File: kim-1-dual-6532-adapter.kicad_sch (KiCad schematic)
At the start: 13 parts, among them J2_1 6530_002_L, J2_2 6530_002_R, J3_1 6530_003_L, J3_2 6530_003_R, U1 27C64, U2 6532, U3 6532, U4 74LS138, U5 74LS00, U6 74LS04

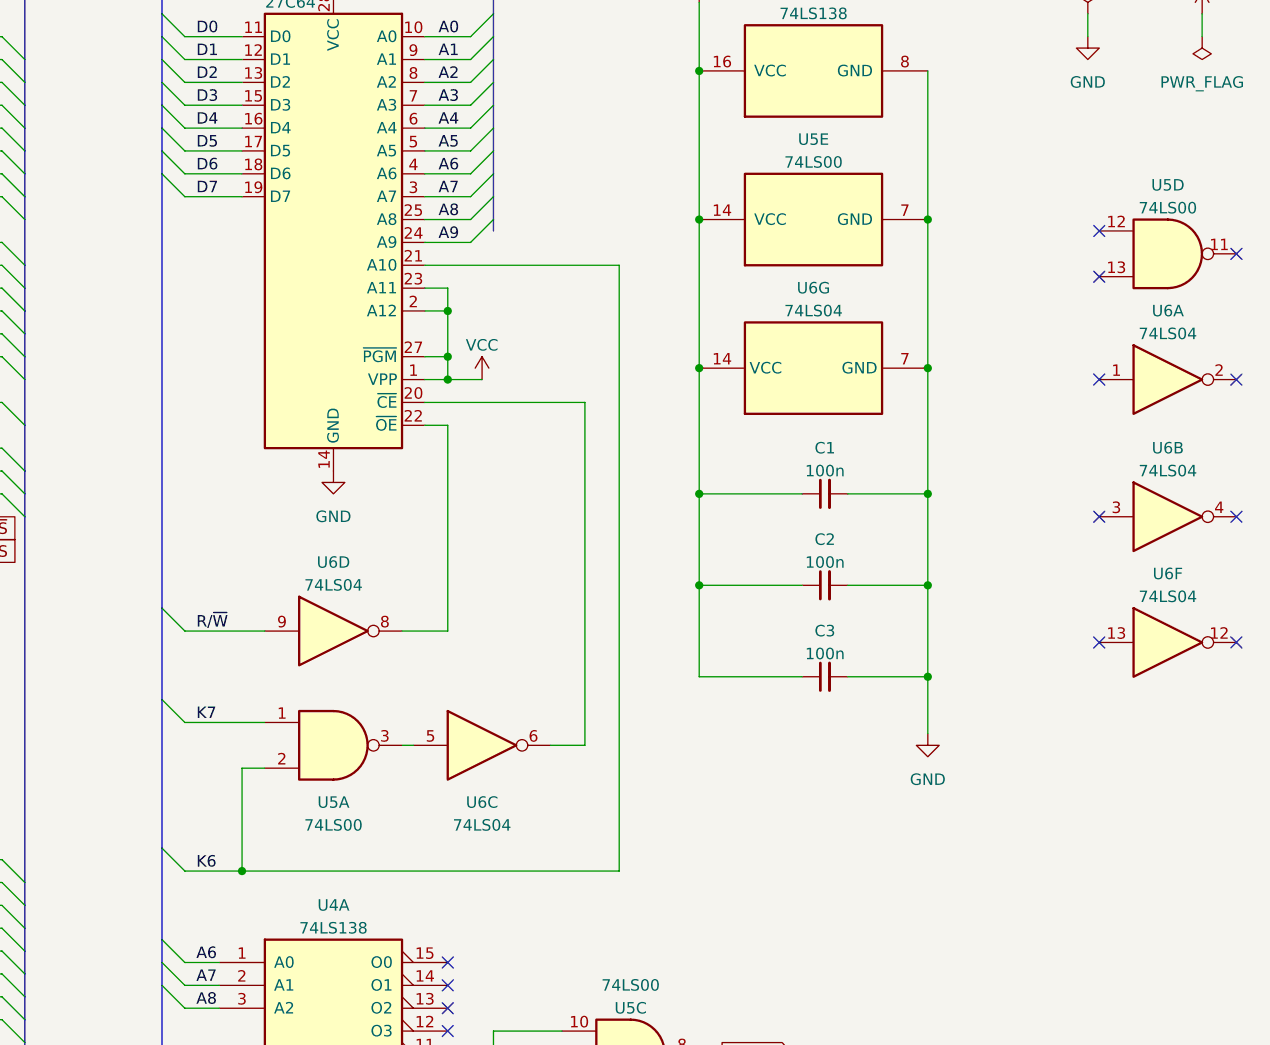
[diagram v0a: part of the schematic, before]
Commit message: Control ROM's OE with phi2
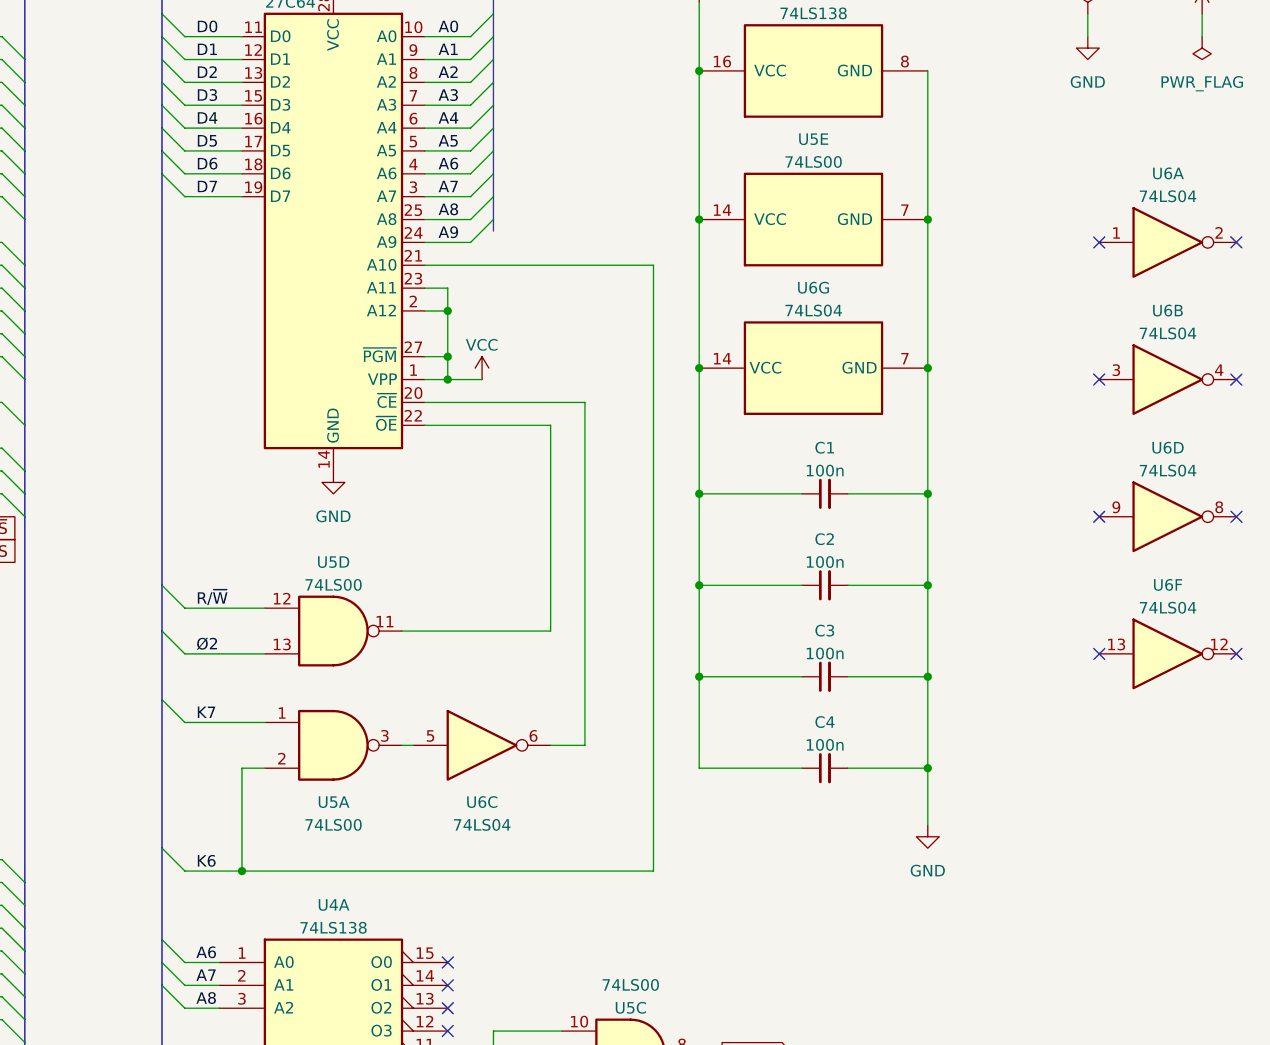
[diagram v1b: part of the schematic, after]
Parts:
- added C4: 100n, KIM-1_Library:C_Disc_D3.0mm_W2.0mm_P2.50mm, symbol Device:C_Small
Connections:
- net GND: now also C4.2
- net R/~{W}: now also U5.12; no longer U6.9
- net VCC: now also C4.1
- net Ø2: now also U5.13
- net at U5.11: now also U1.22 (~{OE})
- net at U6.8: no longer U1.22 (~{OE})
- no-connect marks 17 -> 16
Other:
- moved on the sheet: U5D, U6A, U6B, U6F
